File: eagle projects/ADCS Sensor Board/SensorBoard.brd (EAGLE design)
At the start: 91 x 91 mm, 96 parts, among them J5 HDR_10_EZFET_DEBUGGER, J6 MTI-1_8428-11B1-RK-TP, Q1 BC850SMD, Q2 IRF7507TRPBF, U1 MSP430F5529IPN, U2 LMV321, U3 ADS7841E_2K5, U4 LMV321, U5 LM20BIM7X_NOPB, U6 LMV321, Y1 32.768kHz, Y2 CSTCR4M00G15L99

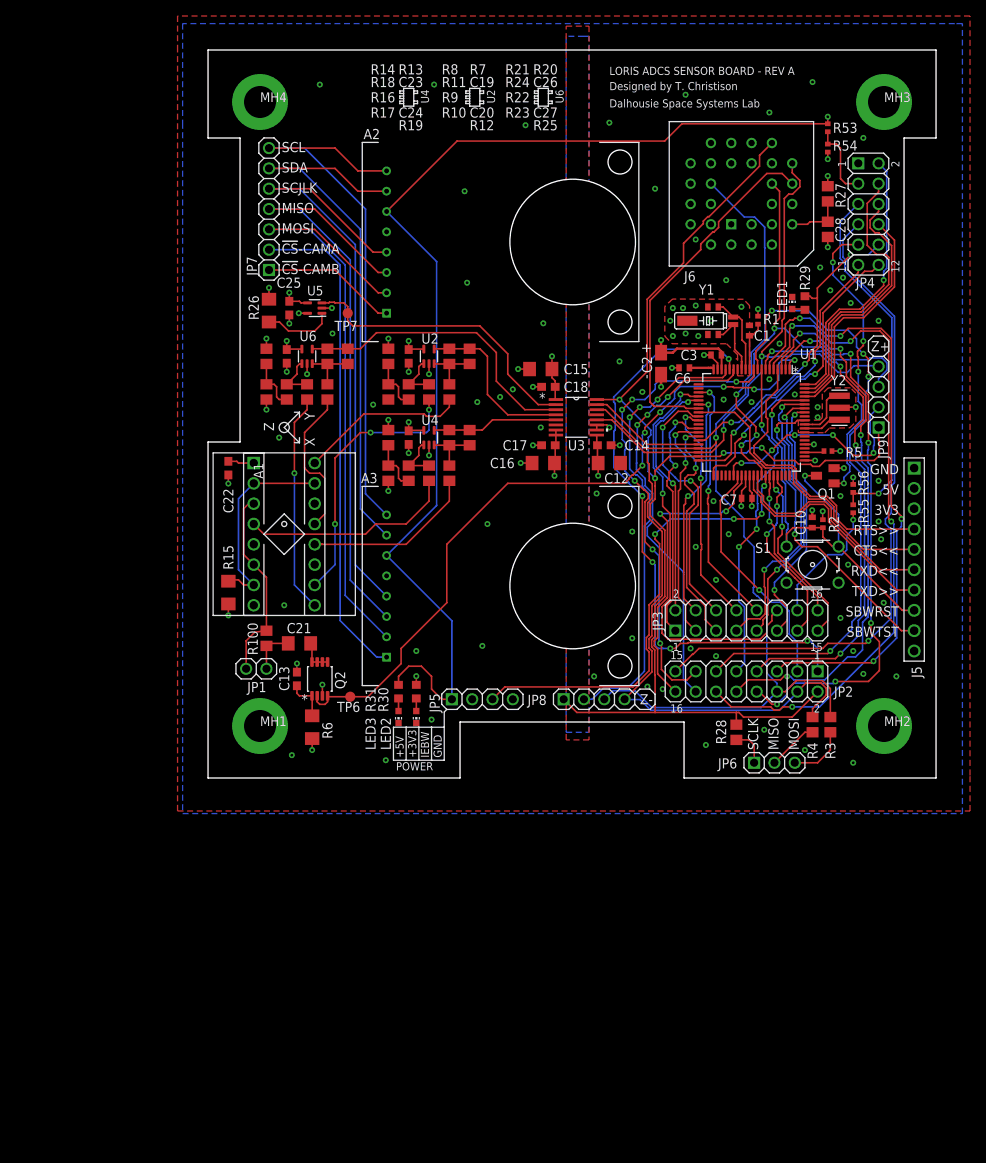
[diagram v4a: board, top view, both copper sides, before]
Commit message: Removed temperature sensor
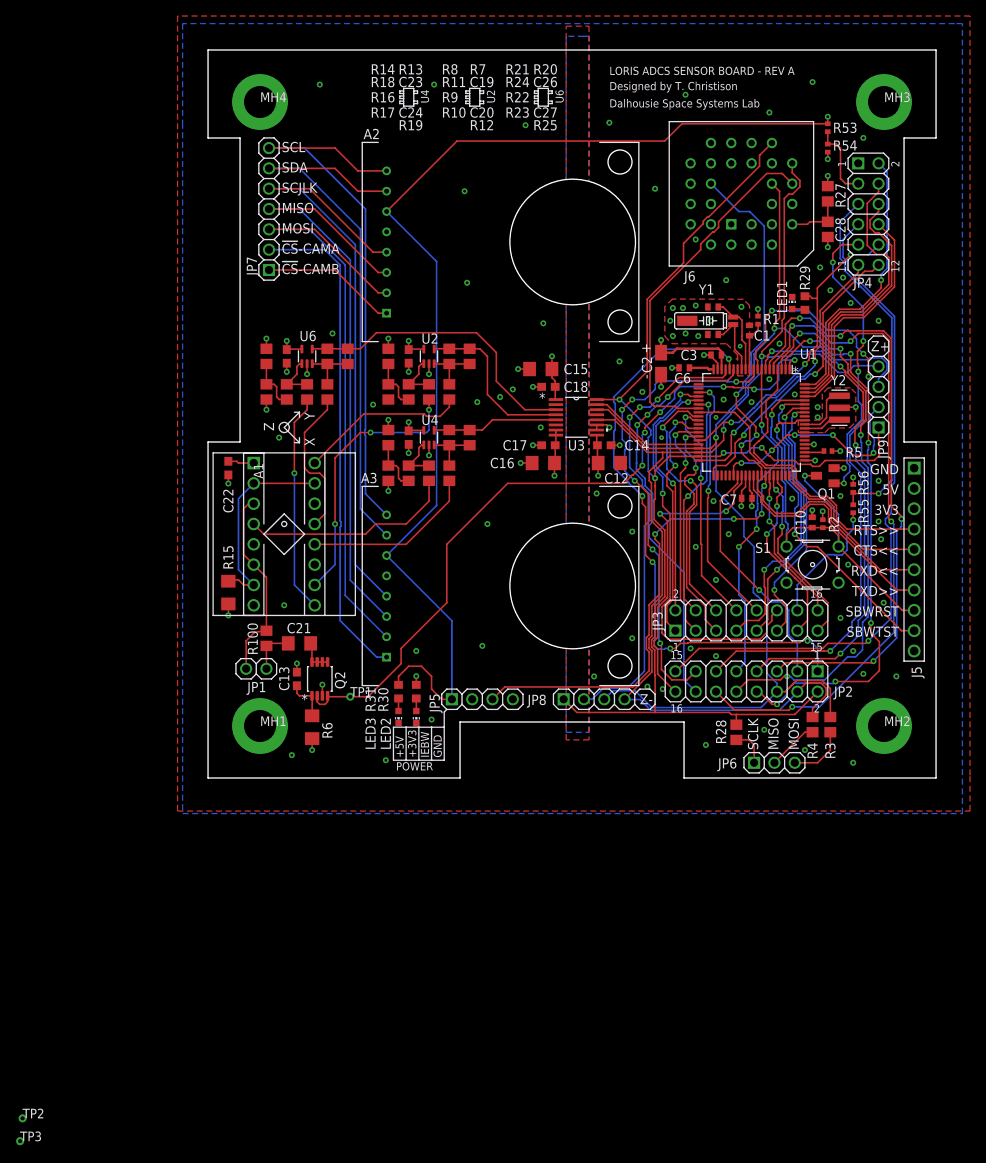
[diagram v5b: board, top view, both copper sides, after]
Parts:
- removed C25: 0.1u, rcl:C0603
- removed R26: 5.1M, resistor:R1206
- removed TP6, TP7: TPB1,27, testpad:B1,27
- removed U5: LM20BIM7X_NOPB, my_library:SOT23-5P65_210X110L40X22N_LM20
- added TP1, TP2, TP3: TESTPOINT, my_library:TP_P76H50
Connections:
- removed net N$40: R26.2, U5.1
- net +3V3: no longer C25.2, U5.4
- net BRD_TEMP_MEAS: no longer TP7.TP, U5.3
- net GND: no longer C25.1, R26.1, U5.2, U5.5
- net HMC1053_RESET: now also TP1.1; no longer TP6.TP
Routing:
- net BRD_TEMP_MEAS: track 37.1 -> 0.00 mm
- net N$40: track 8.76 -> 0.00 mm
- net GND: track 48.8 -> 43.4 mm
- net +3V3: track 59.9 -> 56.4 mm, vias 17 -> 16
- net OUT_B_P: track 22.6 -> 21.6 mm
- net UCB0_SPI_CLK: track 156.8 -> 155.9 mm
- net P5.5/XOUT1: track 9.26 -> 8.42 mm
- net RST/SBWTDIO: track 58.4 -> 57.7 mm
- net N$39: track 6.04 -> 5.47 mm
- net N$7: track 7.63 -> 7.12 mm

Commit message: Added testpoints, updated drill chart
Added missing MTI-1 IMU reset signal to msp430
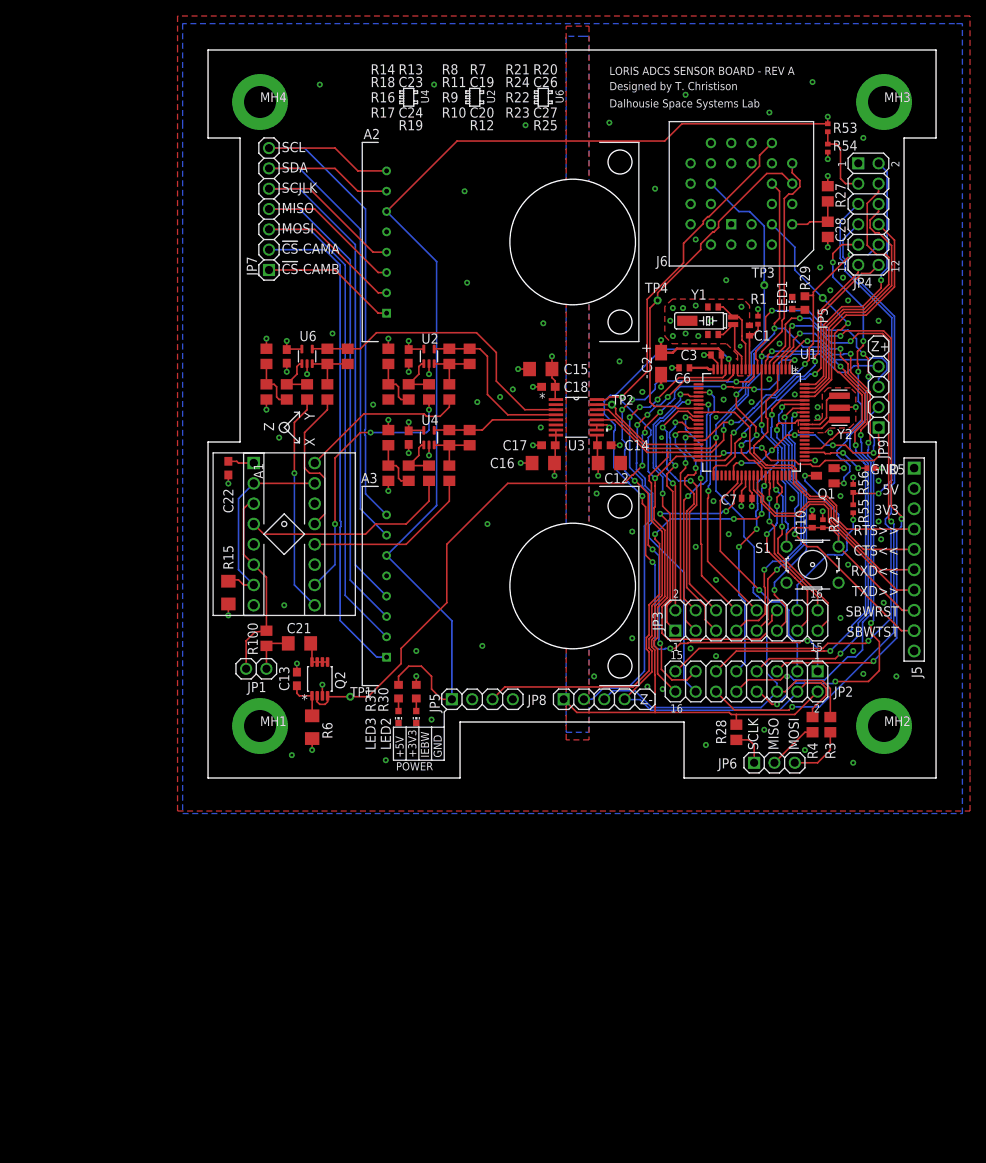
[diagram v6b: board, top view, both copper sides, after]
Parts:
- added TP4, TP5: TESTPOINT, my_library:TP_P76H50
- moved TP3 141.8 mm to (69.5, 61.6)
- moved TP2 115.7 mm to (50.5, 46.7)
- moved R5 5.78 mm to (82.9, 38.7)
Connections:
- removed net BRD_TEMP_MEAS: U3.2
- new net !RST!_MTI: J6.6, TP5.1, U1.64
- net !CS!_HMC1053: now also TP2.1
- net !CS!_MTI: now also TP4.1
- net MTI_DRDY: now also TP3.1
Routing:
- net !RST!_MTI: track 0.00 -> 39.6 mm, vias 0 -> 1
- net TARGET_PUR: track 2.59 -> 8.69 mm, vias 0 -> 2
- net !CS!_SUN_Y-: track 76.5 -> 77.8 mm
- net GND: track 43.4 -> 42.1 mm, vias 112 -> 111
- net MSP_OBC_RESET: track 36.9 -> 38.1 mm
- net MSP430_ACTIVE: track 39.1 -> 38.5 mm
- net !SPEED_CLR: track 62.6 -> 63.1 mm

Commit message: Fixed testpoint silkscreens, moved vias where silk interfered
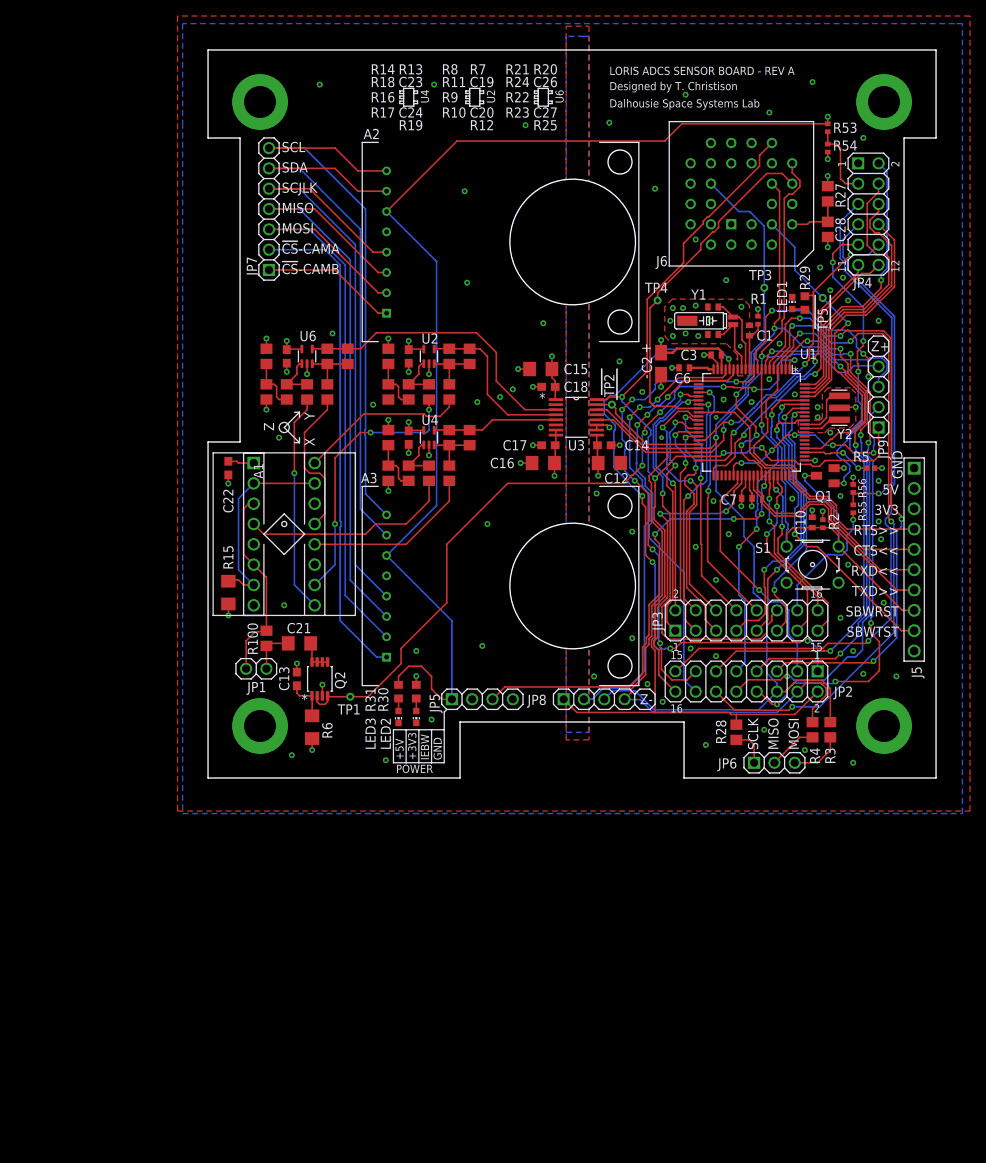
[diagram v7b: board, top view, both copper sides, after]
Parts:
- moved R3 0.64 mm to (77.8, 6.03)
- moved R4 0.64 mm to (75.6, 6.03)
- moved TP3 0.32 mm to (69.5, 61.3)
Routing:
- net UCB0_SPI_MOSI: track 142.8 -> 143.6 mm
- net N$3: track 7.33 -> 6.69 mm
- net UCB0_SPI_MISO: track 140.1 -> 140.6 mm
- net INIT_EPS_BURN_WIRE: track 58.6 -> 58.0 mm

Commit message: Renumbered parts and exported bom CSV
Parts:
- removed C26: 0.1u, rcl:C0603
- removed C27: 1n, rcl:C0805
- removed C28: 470n, rcl:C0805
- removed R100: 0R, rcl:R0805
- removed R53, R55: 1k, rcl:R0402
- removed R54, R56: 2k, rcl:R0402
- added C11: 0.1u, rcl:C0603
- added C8: 100n, rcl:C0402
- added C9: 1u, resistor:C1206
- added R26: 5.6k, rcl:R0805
- added R32: 750R, rcl:R0603
- added R33, R34, R35: 0R, rcl:R0805
- C10: value 1n -> 0.1u; device rcl:C0402 -> rcl:C0603
- C13: value 0.1u -> 1u; device rcl:C0603 -> resistor:C1206
- C15, C16: value 1u -> 0.1u; device resistor:C1206 -> rcl:C0603
- C17, C23: value 0.1u -> 1n; device rcl:C0603 -> rcl:C0805
- C18: value 0.1u -> 1n; device rcl:C0603 -> resistor:C1206
- C20: value 1n -> 0.1u; device rcl:C0805 -> rcl:C0603
- C21: device resistor:C1206 -> rcl:C0805
- C24: value 1n -> 470n
- C3: value 100n -> 12p
- C5: value 12p -> 100n
- C7: value 100n -> 1n
- JP1: device my_library:1X02 -> my_library:1X04
- JP4: device my_library:2X06 -> my_library:1X04
- JP5: device my_library:1X04 -> my_library:2X06
- JP6: device my_library:1X03 -> my_library:1X02
- JP9: device my_library:1X04 -> my_library:1X03
- R10, R17: value 5.6k -> 1k
- R11, R18, R24, R25: value 1.37M -> 1k
- R12: value 1.37M -> 5.6k
- R13, R20, R21: value 1k -> 5.6k
- R14: value 1k -> 1.37M
- R15: value 5.1M -> 1.37M; device resistor:R1206 -> rcl:R0805
- R16: value 5.6k -> 0R
- R19: value 1.37M -> 5.1M; device rcl:R0805 -> resistor:R1206
- R2: value 47k -> 1k
- R22, R23: value 5.6k -> 1.37M
- R27: value 27R -> 5.6k
- R28: value 0R -> 1.37M
- R29: value 470R -> 1.37M; device rcl:R0603 -> rcl:R0805
- R3: value 0R -> 2k; device rcl:R0805 -> rcl:R0402
- R30: value 470R -> 27R; device rcl:R0603 -> rcl:R0805
- R31: value 750R -> 470R
- R4: value 0R -> 1k; device rcl:R0805 -> rcl:R0402
- R5: value 1M -> 2k
- R6: value 200R -> 1M; device resistor:R1206 -> rcl:R0402
- R7: value 1k -> 47k; device rcl:R0805 -> rcl:R0402
- R8: value 1k -> 470R; device rcl:R0805 -> rcl:R0603
- R9: value 5.6k -> 200R; device rcl:R0805 -> resistor:R1206
- moved JP1 84.9 mm to (83.8, 47.6), turned to 90 degrees
- moved R30 80.7 mm to (77.5, 73.0)
- moved JP5 77.5 mm to (82.5, 70.5), turned to 270 degrees
- moved R6 77.0 mm to (82.9, 38.7), turned to 180 degrees
- moved R3 72.7 mm to (77.5, 78.7), turned to 90 degrees
- moved R28 70.5 mm to (9.84, 48.3), turned to 90 degrees
- moved JP4 69.7 mm to (48.3, 9.84), turned to 0 degrees
- moved C10 67.3 mm to (11.1, 12.4), turned to 270 degrees
- moved R27 67.3 mm to (14.9, 48.3)
- moved JP6 65.8 mm to (6.03, 13.7)
- moved R7 58.2 mm to (76.9, 31.8), turned to 90 degrees
- moved R29 57.5 mm to (17.5, 52.7)
- moved C24 54.0 mm to (77.5, 68.6)
- moved R8 53.2 mm to (74.6, 59.4)
- moved R2 49.5 mm to (77.5, 81.3)
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- renumbered J5 to J1, J6 to J2, U6 to U5
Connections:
- net !CS!_SUN_Z+: now also JP1.2; no longer JP9.2
- net !CS!_SUN_Z-: now also JP4.2; no longer JP8.2
- net !RST!_MTI: now also TP3.1; no longer TP5.1
- net +3V3: now also C11.1, C13.1, C20.1, C5.2, C8.1, C9.1, JP5.1, JP8.2, R10.1, R17.1, R24.1, R31.1, R7.2, R9.2; no longer C17.1, C18.1, C23.1, C26.1, C3.2, C7.1, JP4.1, JP5.2, R13.1, R2.2, R20.1, R27.1, R6.2, R7.1
- net +5V: now also JP8.1, R2.2, R32.1; no longer JP5.1, R31.1, R53.2
- net ACT_BRD_3V_PRESENT: now also JP5.7; no longer JP4.7
- net ACT_BRD_5V_PRESENT: now also R4.2; no longer R55.2
- net ACT_BRD_5V_SHIFTED: now also JP5.5, R4.1, R5.2; no longer JP4.5, R55.1, R56.2
- net B_MEAS_X: now also C21.2, R23.1; no longer C24.2, R19.1
- net B_MEAS_Y: now also C17.2, R15.1; no longer C20.2, R12.1
- net B_MEAS_Z: now also C23.2, R29.1; no longer C27.2, R25.1
- net GND: now also C10.1, C11.2, C13.2, C20.2, C24.1, C8.2, C9.2, JP8.4, R11.2, R18.2, R19.1, R25.2, R3.1, R6.1; no longer C10.2, C13.1, C17.2, C18.2, C23.2, C26.2, C28.1, JP5.4, R14.2, R15.1, R21.2, R54.1, R56.1, R8.2
- net INIT_EPS_BURN_WIRE: now also JP8.3; no longer JP5.3
- net MSP430_ACTIVE: now also JP5.10, R8.1; no longer JP4.10, R29.1
- net MSP_OBC_RESET: now also JP5.9; no longer JP4.9
- net MTI_DRDY: now also TP5.1; no longer TP3.1
- net N$1: now also JP9.1, R33.2; no longer JP6.1, R28.2
- net N$2: now also JP9.2, R34.2; no longer JP6.2, R4.2
- net N$20: now also R10.2, R14.1; no longer R7.2, R8.1
- net N$21: now also C17.1, R13.1, R15.2; no longer C20.1, R10.1, R12.2
- net N$23: now also R12.1, R14.2; no longer R11.2, R9.1
- net N$3: now also JP9.3, R35.2; no longer JP6.3, R3.2
- net N$35: now also C18.2, JP6.2, R16.1; no longer C21.2, JP1.2, R100.1
- net N$36: now also R19.2; no longer R15.2
- net N$37: now also JP6.1, R16.2; no longer JP1.1, R100.2
- net N$38: now also C18.1; no longer C21.1
- net N$39: now also C10.2, R9.1; no longer C13.2, R6.1
- net N$4: now also R8.2; no longer R29.2
- net N$49: now also R17.2, R22.1; no longer R13.2, R14.1
- net N$5: now also R31.2; no longer R30.2
- net N$50: now also C21.1, R21.1, R23.2; no longer C24.1, R17.1, R19.2
- net N$52: now also R20.1, R22.2; no longer R16.1, R18.2
- net N$59: now also R24.2, R25.1, R28.1; no longer R20.2, R21.1, R24.1
- net N$6: now also R32.2; no longer R31.2
- net N$60: now also C23.1, R27.1, R29.2; no longer C27.1, R23.1, R25.2
- net N$62: now also R26.1, R28.2; no longer R22.1, R24.2
- net N$7: now also C24.2, R30.2; no longer C28.2, R27.2
- net OUT_A_N: now also R12.2; no longer R9.2
- net OUT_A_P: now also R13.2; no longer R10.2
- net OUT_B_N: now also R20.2; no longer R16.2
- net OUT_B_P: now also R21.2; no longer R17.2
- net OUT_C_N: now also R26.2; no longer R22.2
- net OUT_C_P: now also R27.2; no longer R23.2
- net P5.4/XIN1: now also C3.2; no longer C4.2
- net P5.5/XOUT1: now also C4.2; no longer C5.2
- net RESERVED_1: now also JP5.2; no longer JP4.2
- net RESERVED_2: now also JP5.4; no longer JP4.4
- net RESERVED_3: now also JP5.6; no longer JP4.6
- net RESERVED_4: now also JP5.8; no longer JP4.8
- net RST/SBWTDIO: now also C7.1, R7.1; no longer C10.1, R2.1
- net SEN_BRD_5V_PRESENT: now also JP5.3, R2.1, R3.2; no longer JP4.3, R53.1, R54.2
- net TARGET_PUR: now also R6.2; no longer R5.2
- net UCA0RXD: now also JP5.12; no longer JP4.12
- net UCA0TXD: now also JP5.11; no longer JP4.11
- net UCB0_SPI_CLK: now also JP1.1, JP4.1, R33.1; no longer JP8.1, JP9.1, R28.1
- net UCB0_SPI_MISO: now also JP1.4, JP4.4, R34.1; no longer JP8.4, JP9.4, R4.1
- net UCB0_SPI_MOSI: now also JP1.3, JP4.3, R35.1; no longer JP8.3, JP9.3, R3.1
